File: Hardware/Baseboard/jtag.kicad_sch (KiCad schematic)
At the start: 3 parts, among them J1 USB_C_Receptacle_USB2.0_16P, U1 LFE5UM5G-85F-8BG381x, U3 FT2232HL

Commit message: some schematics update
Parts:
- removed J1: USB_C_Receptacle_USB2.0_16P, symbol Connector:USB_C_Receptacle_USB2.0_16P
- removed U1: LFE5UM5G-85F-8BG381x, Package_BGA:Lattice_caBGA-381_17.0x17.0mm_Layout20x20_P0.8mm_Ball0.4mm_Pad0.4mm_NSMD, symbol FPGA_Lattice:LFE5UM5G-85F-8BG381x
- added J3: USB_C_Receptacle_USB2.0_16P, Connector_USB:USB_C_Receptacle_GCT_USB4110, symbol Connector:USB_C_Receptacle_USB2.0_16P
- added R3, R4: 5k1, Resistor_SMD:R_0805_2012Metric, symbol Device:R
- added U1: 93LCxxC, symbol Memory_EEPROM:93LCxxC
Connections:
- net GND: now reaches U3.1 (GND)
- net GND: now also U3.10 (AGND), U3.11 (GND), U3.13 (TEST), U3.15 (GND), U3.25 (GND), U3.35 (GND), U3.47 (GND), U3.5 (GND), U3.51 (GND), U1.5 (GND)
- net +3.3V: now reaches U3.12 (VCORE)
- net +3.3V: now also U3.37 (VCORE), U3.64 (VCORE), U1.6 (ORG), U1.8 (VCC)
- net +1.8V: now reaches U3.20 (VCCIO)
- net +1.8V: now also U3.31 (VCCIO), U3.42 (VCCIO), U3.56 (VCCIO)
- net at U3.61 (EEDATA): now also U1.3 (DI)
- net at U3.62 (EECLK): now also U1.2 (SCLK)
- net at U3.63 (EECS): now also U1.1 (CS)
- net at U3.7 (DM): now also J3.A7 (D-), J3.B7 (D-)
- net at U3.8 (DP): now also J3.A6 (D+), J3.B6 (D+)
- new net: J3.B5 (CC2), R4.2
- new net: J3.A5 (CC1), R3.2
- new net +5V_USB: J3.A4 (VBUS), J3.A9 (VBUS), J3.B4 (VBUS), J3.B9 (VBUS)
- new net GND1: J3.A1 (GND), J3.A12 (GND), J3.B1 (GND), J3.B12 (GND), J3.S1 (SHIELD), R3.1, R4.1
- no-connect marks 0 -> 2

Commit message: Baseboard: JTAG
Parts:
- added C1, C10, C11, C13, C15, C17, C4, C5, C6, C7, C9: 100nF, Capacitor_SMD:C_0402_1005Metric, symbol RA8M1:885012205092
- added C12, C14, C16: 4.7uF, Capacitor_SMD:C_0402_1005Metric, symbol RA8M1:885012205092
- added C2, C3: 27pF, Capacitor_SMD:C_0402_1005Metric, symbol RA8M1:885012205092
- added C8: 10uF, Capacitor_SMD:C_0402_1005Metric, symbol RA8M1:885012205092
- added L1, L2, L3: 600R 500mA, symbol Device:L
- added R1, R8: 5k1, Resistor_SMD:R_0402_1005Metric, symbol Device:R
- added R10, R11, R9: 4.7k, Resistor_SMD:R_0402_1005Metric, symbol Device:R
- added R12, R13, R2, R7: 2.2k, Resistor_SMD:R_0402_1005Metric, symbol Device:R
- added R14, R15, R16, R17, R18: 0R, Resistor_SMD:R_0402_1005Metric, symbol Device:R
- added R20, R6: 10k, Resistor_SMD:R_0402_1005Metric, symbol Device:R
- added R5: 12k, Resistor_SMD:R_0402_1005Metric, symbol Device:R
- added Y1: 12MHz, Crystal:Crystal_SMD_3225-4Pin_3.2x2.5mm, symbol Device:Crystal_GND24
- R3, R4: value 5k1 -> 10k; footprint Resistor_SMD:R_0805_2012Metric -> Resistor_SMD:R_0402_1005Metric; MPN 560112120019 -> 560112110020
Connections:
- net +1.8V: now also U3.12 (VCORE), U3.37 (VCORE), U3.49 (VREGOUT), U3.64 (VCORE), C10.2, C11.2, C12.2, C9.2; no longer U3.20 (VCCIO), U3.31 (VCCIO), U3.42 (VCCIO), U3.56 (VCCIO)
- net +3.3V: now also R3.1, R4.1, U3.20 (VCCIO), U3.31 (VCCIO), U3.42 (VCCIO), U3.50 (VREGIN), U3.56 (VCCIO), C1.2, C4.2, C5.2, C6.2, C7.2, C8.2, L1.1, L2.1, R20.1, R6.1; no longer U3.12 (VCORE), U3.37 (VCORE), U3.64 (VCORE)
- net +5V_USB: now also C17.1, L3.2; no longer J3.A4 (VBUS), J3.A9 (VBUS), J3.B4 (VBUS), J3.B9 (VBUS)
- net GND: now also J3.A1 (GND), J3.A12 (GND), J3.B1 (GND), J3.B12 (GND), J3.S1 (SHIELD), C1.1, C10.1, C11.1, C12.1, C13.1, C14.1, C15.1, C16.1, C17.2, C2.1, C3.1, C4.1, C5.1, C6.1, C7.1, C8.1, C9.1, R1.1, R5.1, R7.2, R8.1, Y1.2, Y1.4
- net at R4.2: now also U1.1 (CS), U3.63 (EECS); no longer J3.B5 (CC2)
- net at U1.2 (SCLK), U3.62 (EECLK): now also R3.2
- net at U1.3 (DI), U3.61 (EEDATA): now also R12.2
- net at U1.4 (DO): now also R12.1, R20.2
- net at U3.14 (~{RESET}): now also R6.2
- net JTAG_TCK: now reaches U3.16 (ADBUS0)
- net JTAG_TCK: now also R7.1
- net JTAG_TDI: now reaches U3.17 (ADBUS1)
- net JTAG_TDI: now also R9.1
- net JTAG_TDO: now reaches U3.18 (ADBUS2)
- net JTAG_TDO: now also R10.1
- net JTAG_TMS: now reaches U3.19 (ADBUS3)
- net JTAG_TMS: now also R11.1
- net at U3.2 (OSCI): now also C2.2, Y1.3
- net at U3.3 (OSCO): now also C3.2, Y1.1
- net at U3.38 (BDBUS0): now also R14.1, R16.1, R2.2
- net at U3.39 (BDBUS1): now also R13.2, R15.1, R17.1
- net at U3.4 (VPHY): now also C13.2, C14.2, L2.2
- net at U3.40 (BDBUS2): now also R18.1
- net at U3.6 (REF): now also R5.2
- net at U3.9 (VPLL): now also C15.2, C16.2, L1.2
- net at J3.A5 (CC1): now also R8.2; no longer R3.2
- removed net GND1: J3.A1 (GND), J3.A12 (GND), J3.B1 (GND), J3.B12 (GND), J3.S1 (SHIELD), R3.1, R4.1
- new net: J3.B5 (CC2), R1.2
- new net: J3.A4 (VBUS), J3.A9 (VBUS), J3.B4 (VBUS), J3.B9 (VBUS), L3.1
- new net +VCCIO8: R10.2, R11.2, R13.1, R2.1, R9.2
- new net FT_SCL: R16.2
- new net FT_SDA: R17.2, R18.2
- new net FT_UART_RxD: R15.2
- new net FT_UART_TxD: R14.2
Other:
- moved on the sheet: J3, U1, U3

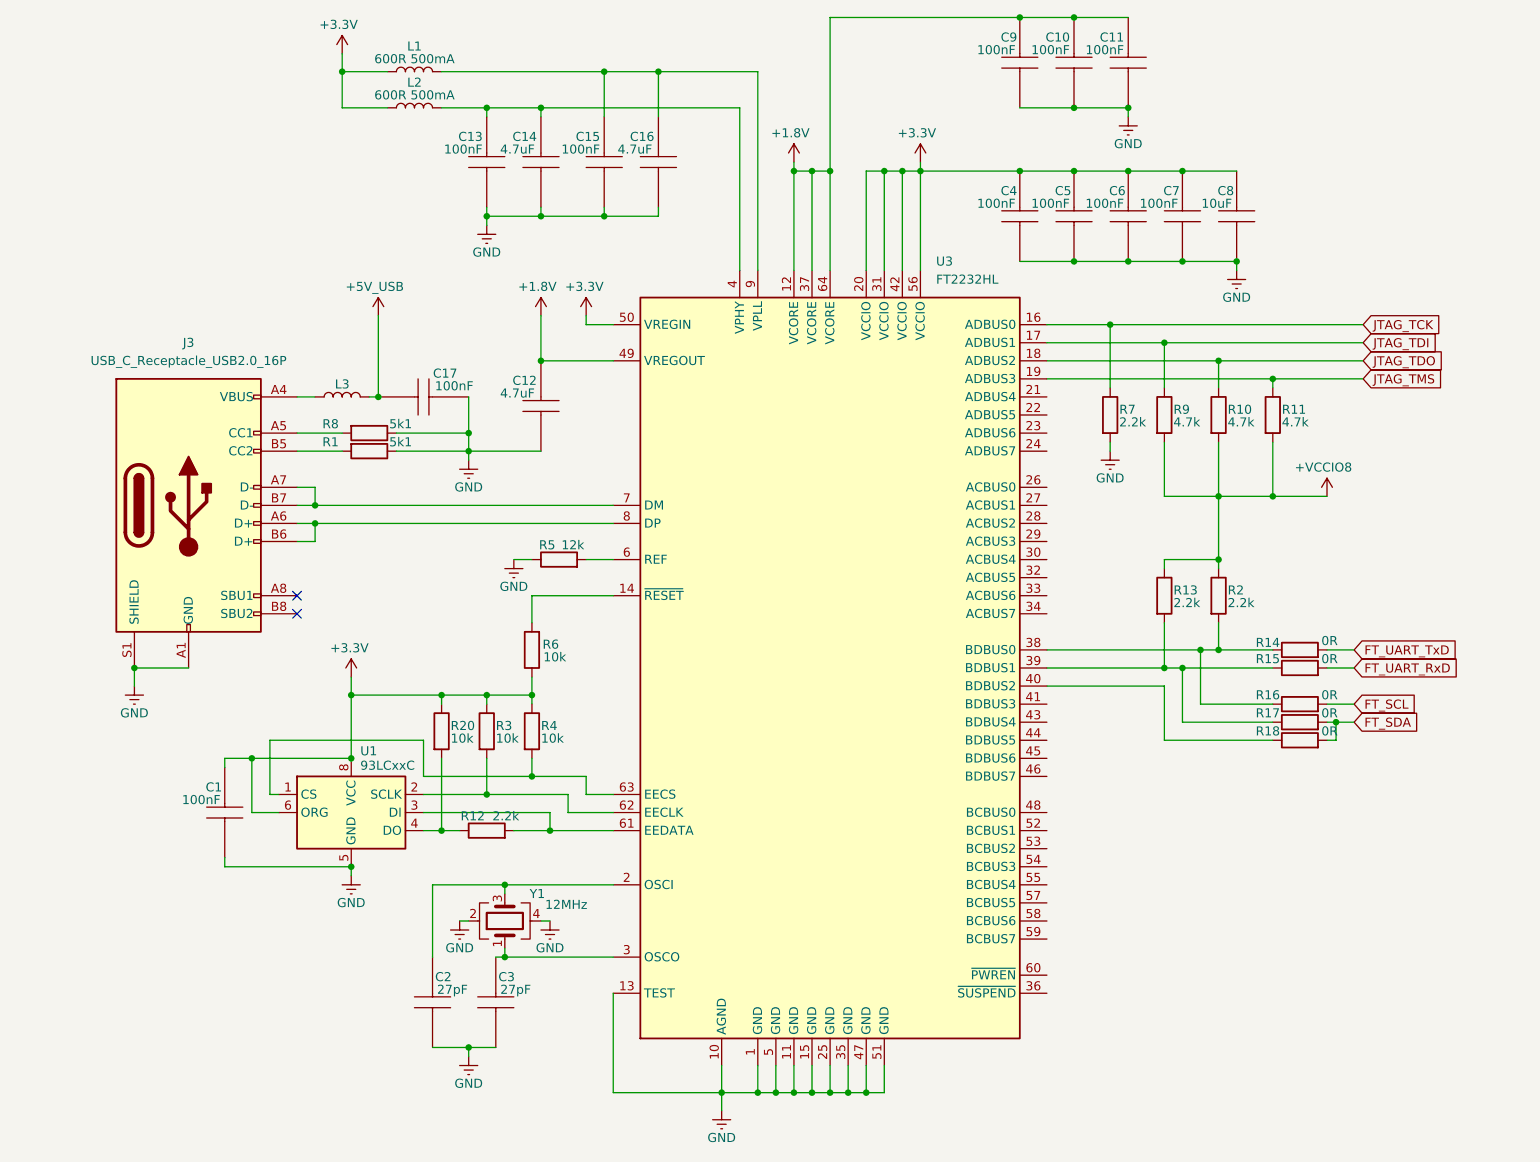
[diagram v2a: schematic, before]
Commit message: QSPI, banks IO decoupling
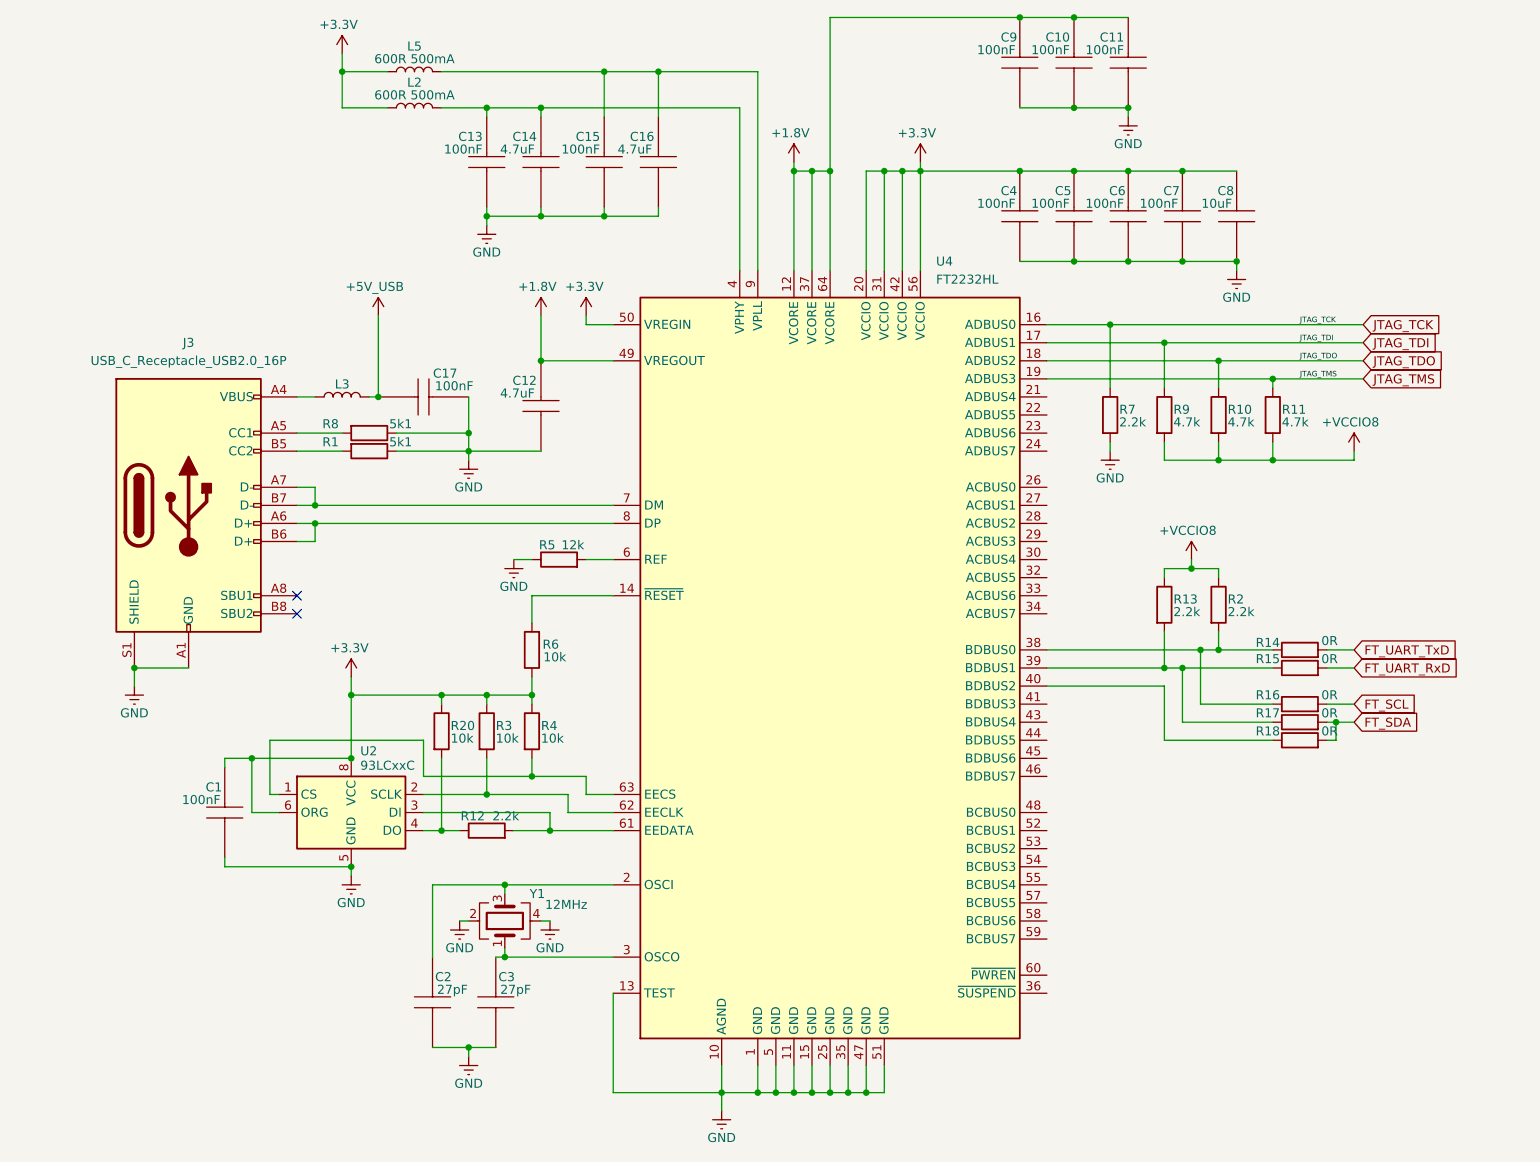
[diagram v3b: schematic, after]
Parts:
- renumbered L1 to L5, U1 to U2, U3 to U4
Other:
- moved on the sheet: R13, R2

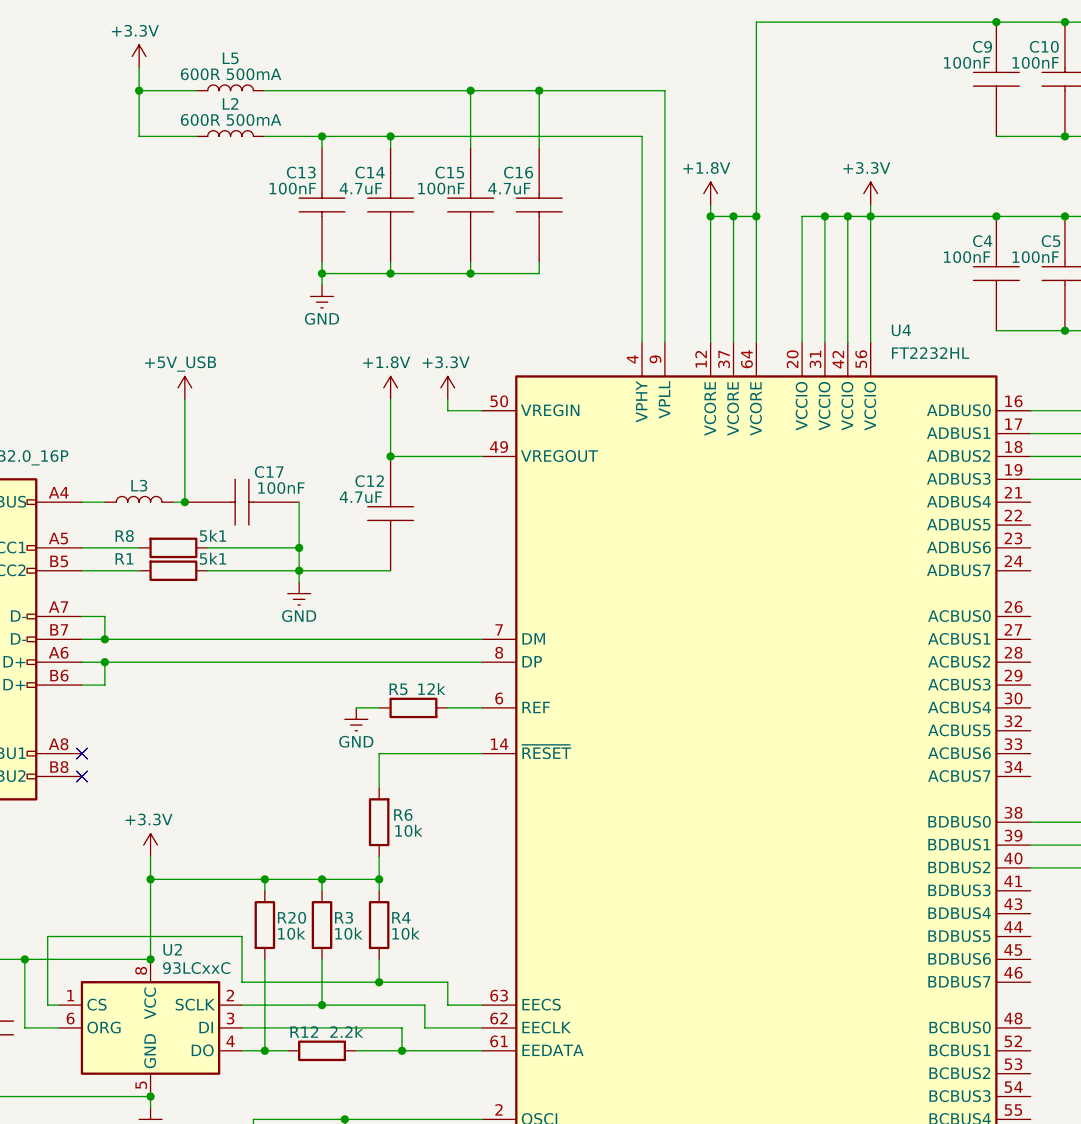
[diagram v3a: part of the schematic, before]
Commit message: M.2 connector added
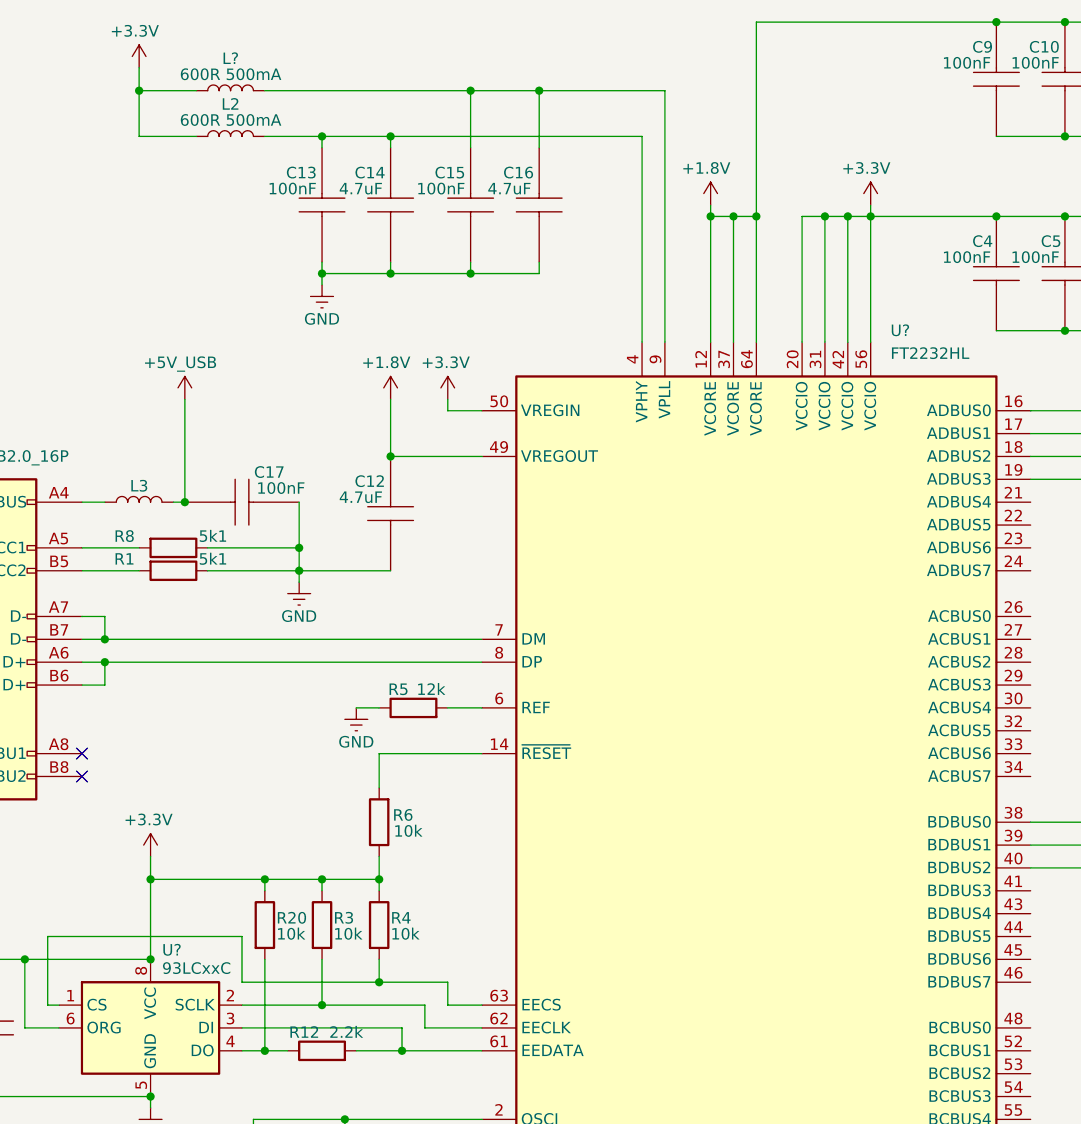
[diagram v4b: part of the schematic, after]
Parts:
- renumbered L5 to L?, U2 to U?, U4 to U?
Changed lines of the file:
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@@
 		(on_board yes)
 		(dnp no)
-		(property "Reference" "U2"
+		(property "Reference" "U?"
 			(at 78.74 120.904 0)
 			(effects
@@
 		)
 		(pin "4"
+		)
+		(instances
+			(project "FPGA4RISCV_BB"
+				(path "/de32abb0-ff3b-4c67-a91a-eed08140b1b2/e8a9a6a8-2e08-4606-b058-44f01919fc3b"
+					(reference "U?")
+					(unit 1)
+				)
+			)
 		)
 	)
@@
 		(dnp no)
 		(fields_autoplaced yes)
-		(property "Reference" "U4"
+		(property "Reference" "U?"
 			(at 159.6741 52.07 0)
 			(effects
@@
 		)
 		(pin "9"
+		)
+		(instances
+			(project "FPGA4RISCV_BB"
+				(path "/de32abb0-ff3b-4c67-a91a-eed08140b1b2/e8a9a6a8-2e08-4606-b058-44f01919fc3b"
+					(reference "U?")
+					(unit 1)
+				)
+			)
 		)
 	)
@@
 		(on_board yes)
 		(dnp no)
-		(property "Reference" "L5"
+		(property "Reference" "L?"
 			(at 86.36 21.844 90)
 			(effects
@@
 		(pin "1"
 		)
+		(instances
+			(project "FPGA4RISCV_BB"
+				(path "/de32abb0-ff3b-4c67-a91a-eed08140b1b2/e8a9a6a8-2e08-4606-b058-44f01919fc3b"
+					(reference "L?")
+					(unit 1)
+				)
+			)
+		)
 	)
